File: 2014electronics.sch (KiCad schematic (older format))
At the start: 31 parts, among them J1 PP15, J10 PP15, J11 PP45, J12 PP45, J13 PP45, J14 PP45, J15 PP15, J16 PP15, J17 PP15, J18 PP15, J19 PP15, J2 PP15, J20 PP30, J21 PP30, J22 PP15, J3 PP15, J4 PP15, J5 PP15, J6 PP45, J7 PP45, J8 PP30, J9 PP30, P1 CONN_2, P2 CONN_2, P3 CONN_2, P4 CONN_2, P5 CONN_2X2, P6 CONN_2, P7 CONN_3X2, P8 CONN_3X2, P9 CONN_3X2

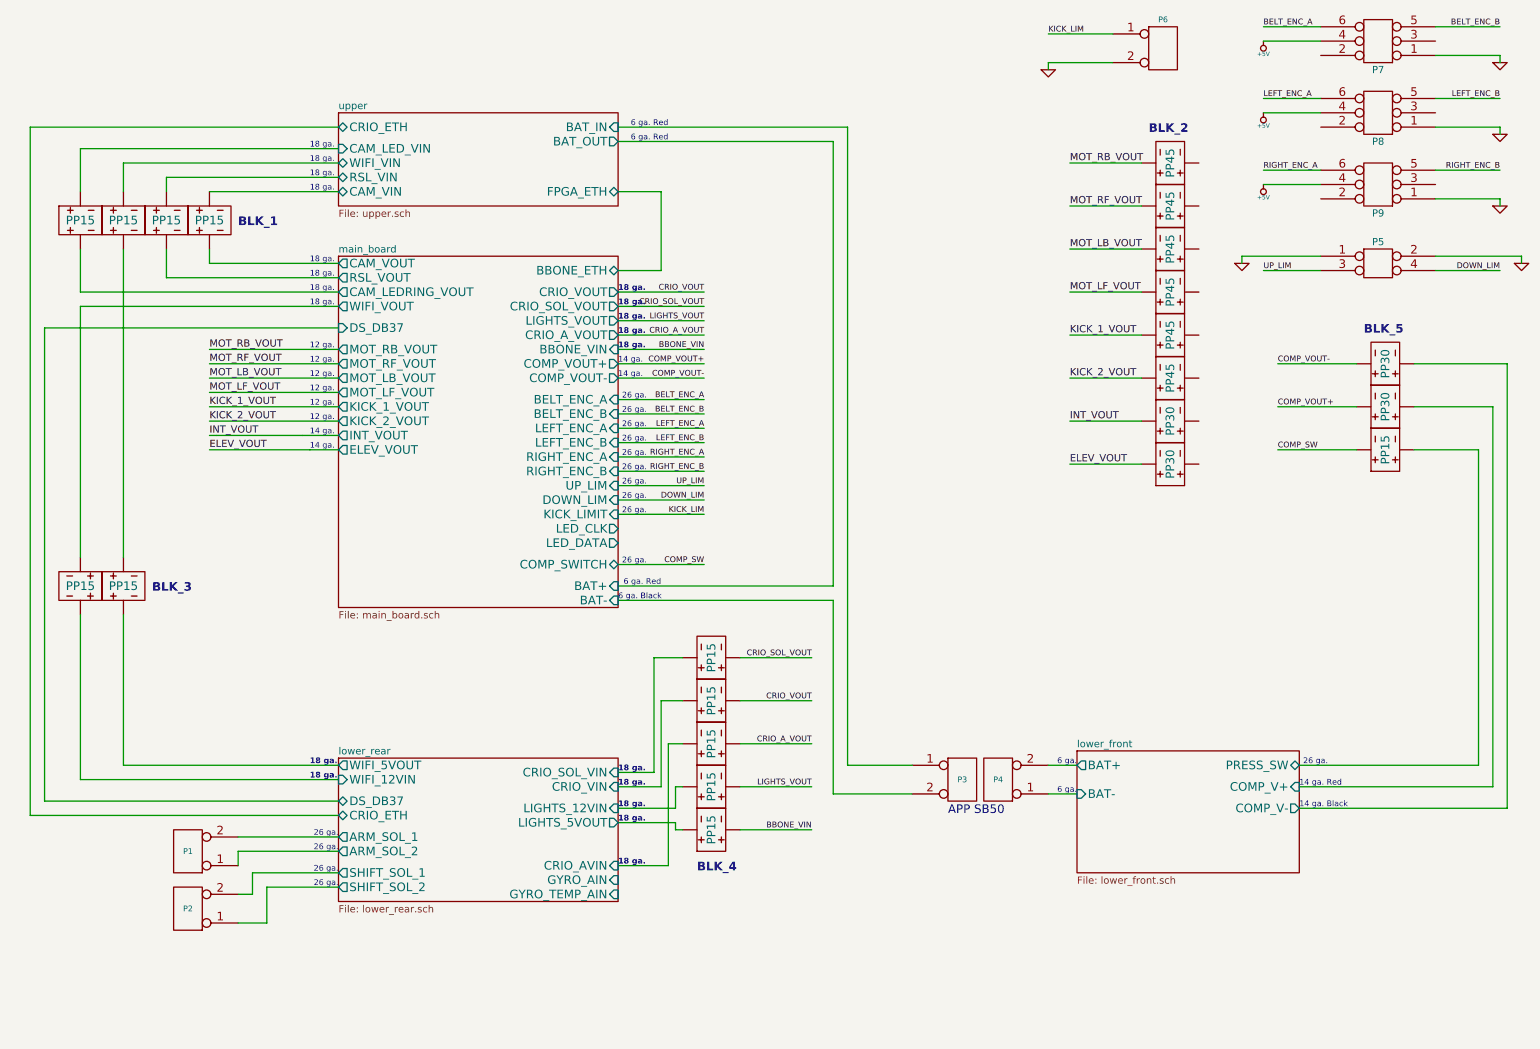
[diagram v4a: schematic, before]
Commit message: Modified layout of main board components.  Replaced more wires with net labels.
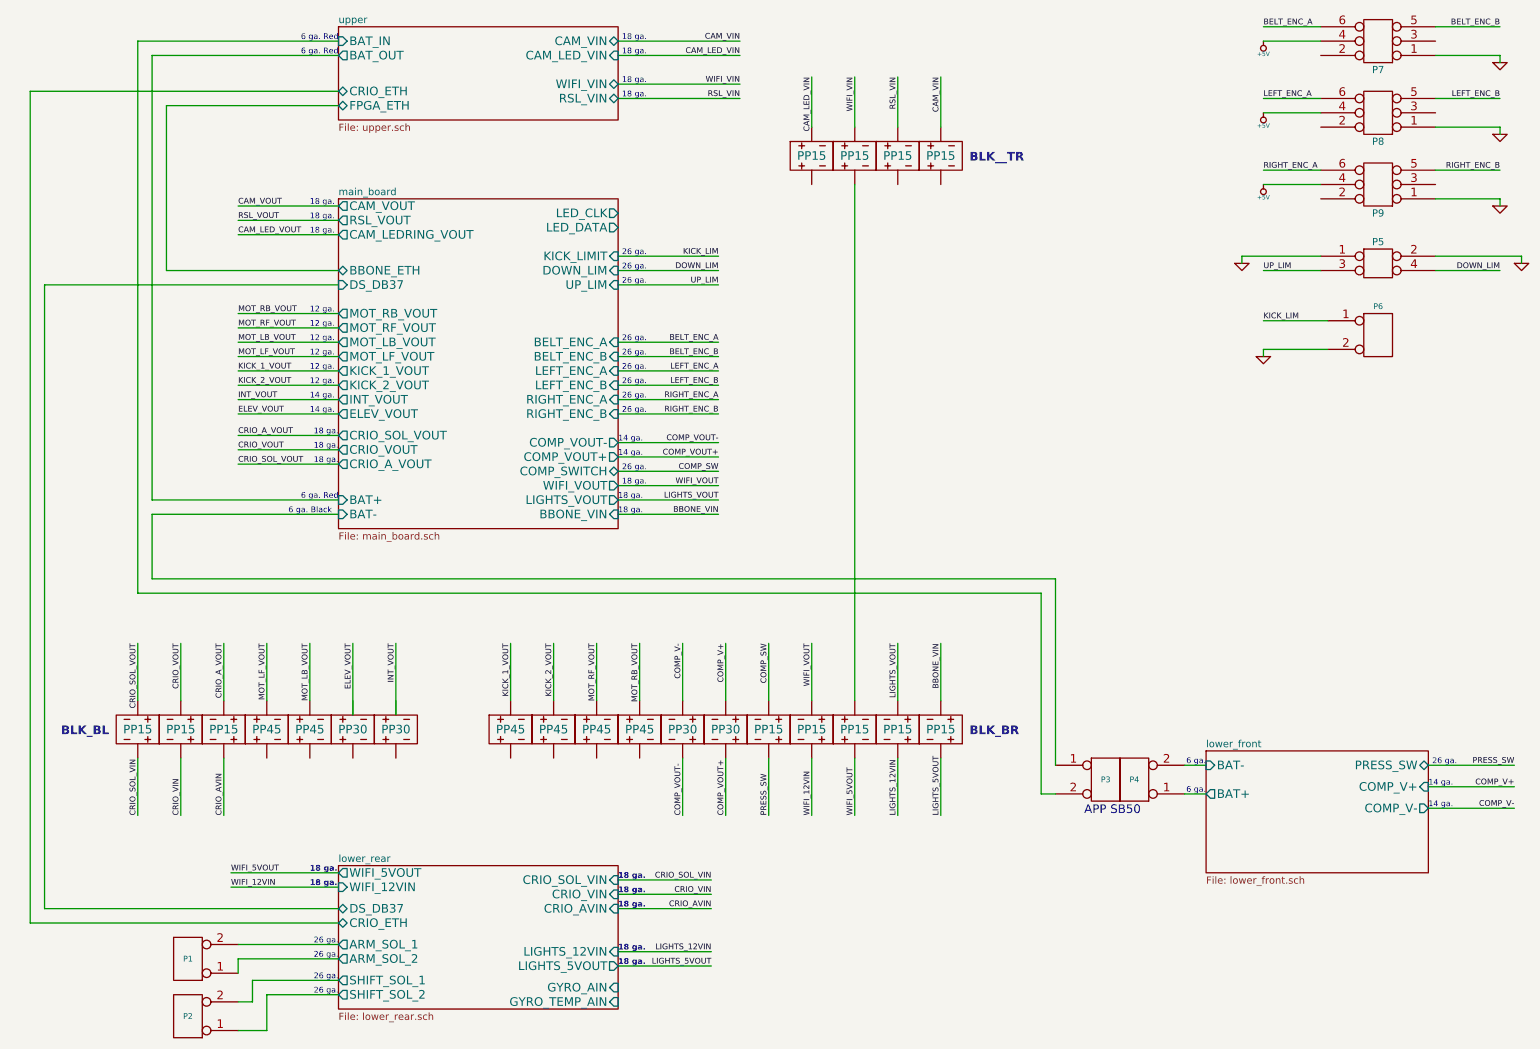
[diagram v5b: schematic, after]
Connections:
- net lower_front/COMP_V+ is gone; now on net COMP_VOUT+: J21.~
- net lower_front/COMP_V- is gone; now on net COMP_VOUT-: J20.~
- net lower_rear/CRIO_AVIN is gone; now on net CRIO_A_VOUT: J17.~
- net lower_rear/CRIO_SOL_VIN is gone; now on net CRIO_SOL_VOUT: J15.~
- net lower_rear/CRIO_VIN is gone; now on net CRIO_VOUT: J16.~
- net lower_rear/LIGHTS_12VIN is gone; now on net LIGHTS_VOUT: J18.~
- net lower_rear/WIFI_5VOUT is gone; now on net WIFI_5VOUT: J4.~
- net main_board/WIFI_VOUT is gone; now on net WIFI_VOUT: J2.~
- net upper/CAM_LED_VIN is gone; now on net CAM_LED_VIN: J1.~
- net upper/CAM_VIN is gone; now on net CAM_VIN: J10.~
- net upper/RSL_VIN is gone; now on net RSL_VIN: J5.~
- net ELEV_VOUT: no longer J9.~
- net INT_VOUT: no longer J8.~
- net KICK_1_VOUT: now also J7.~; no longer J6.~
- net KICK_2_VOUT: now also J6.~; no longer J7.~
- net lower_front/BAT+: now also P4.1 (P1); no longer P4.2 (PM)
- net lower_front/BAT-: now also P4.2 (PM); no longer P4.1 (P1)
- net main_board/BAT-: now also P3.1 (P1); no longer P3.2 (PM)
- net upper/BAT_IN: now also P3.2 (PM); no longer P3.1 (P1)
- net WIFI_5VOUT: now reaches J4.~
- net WIFI_5VOUT: no longer J3.~
- net lower_front/PRESS_SW renamed PRESS_SW
- net lower_rear/LIGHTS_5VOUT renamed LIGHTS_5VOUT
- net lower_rear/WIFI_12VIN renamed WIFI_VOUT
- net main_board/CAM_LEDRING_VOUT renamed CAM_LED_VIN
- net main_board/CAM_VOUT renamed CAM_VIN
- net main_board/RSL_VOUT renamed RSL_VIN
- net upper/WIFI_VIN renamed WIFI_VIN
- new net: J3.~, J4.~
- new net COMP_V+: J21.~
- new net COMP_V-: J20.~
- new net CRIO_AVIN: J17.~
- new net CRIO_SOL_VIN: J15.~
- new net CRIO_VIN: J16.~
- new net LIGHTS_12VIN: J18.~
- new net WIFI_12VIN: J2.~
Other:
- note added: "BLK_BL"
- note added: "BLK_BR"
- note added: "BLK__TR"
- note removed: "14 ga. Black"
- note removed: "14 ga. Red"
- note removed: "BLK_1"
- note removed: "BLK_2"
- note removed: "BLK_3"
- note removed: "BLK_4"
- note removed: "BLK_5"
- moved on the sheet: P1, P2, P3, P4, P6
